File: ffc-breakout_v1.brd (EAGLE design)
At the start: 29.2 x 22.9 mm, 5 parts, among them X2 AMP_SFW16R-2STE1LF

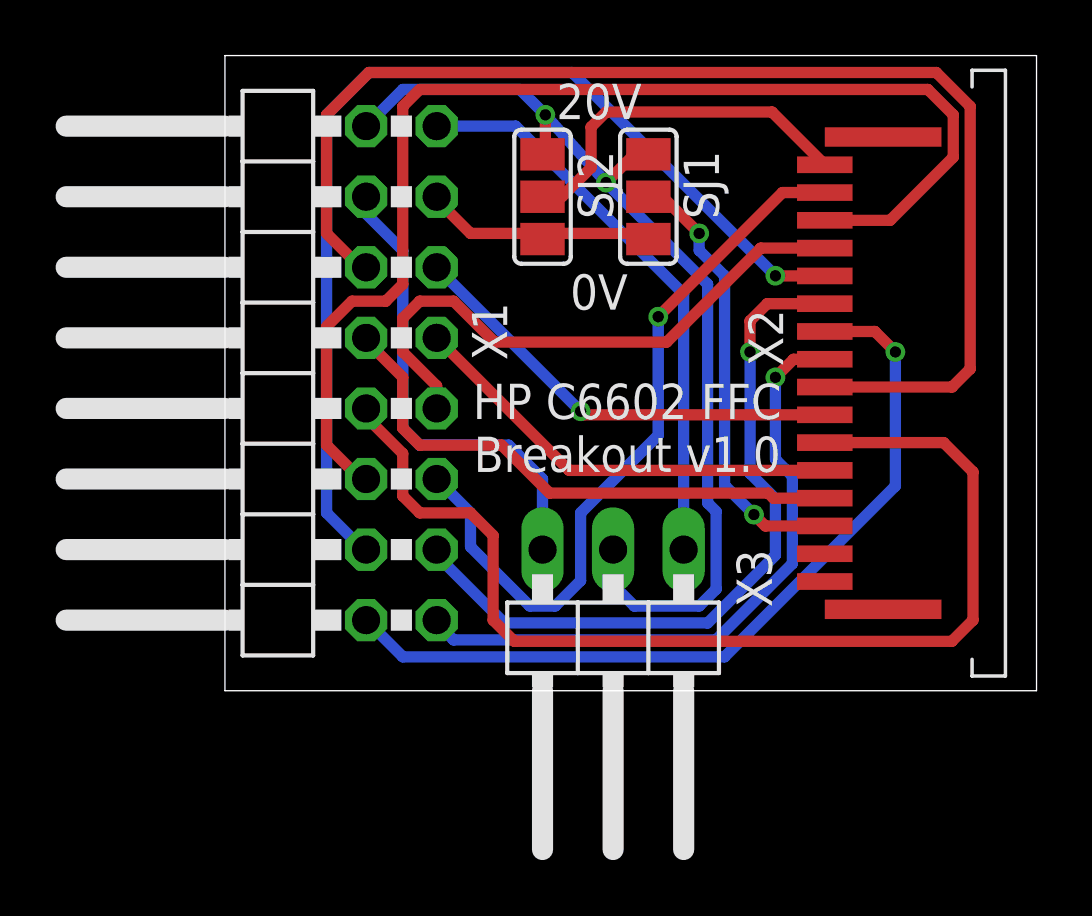
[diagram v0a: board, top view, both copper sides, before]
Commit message: BOM  + minor FFC update
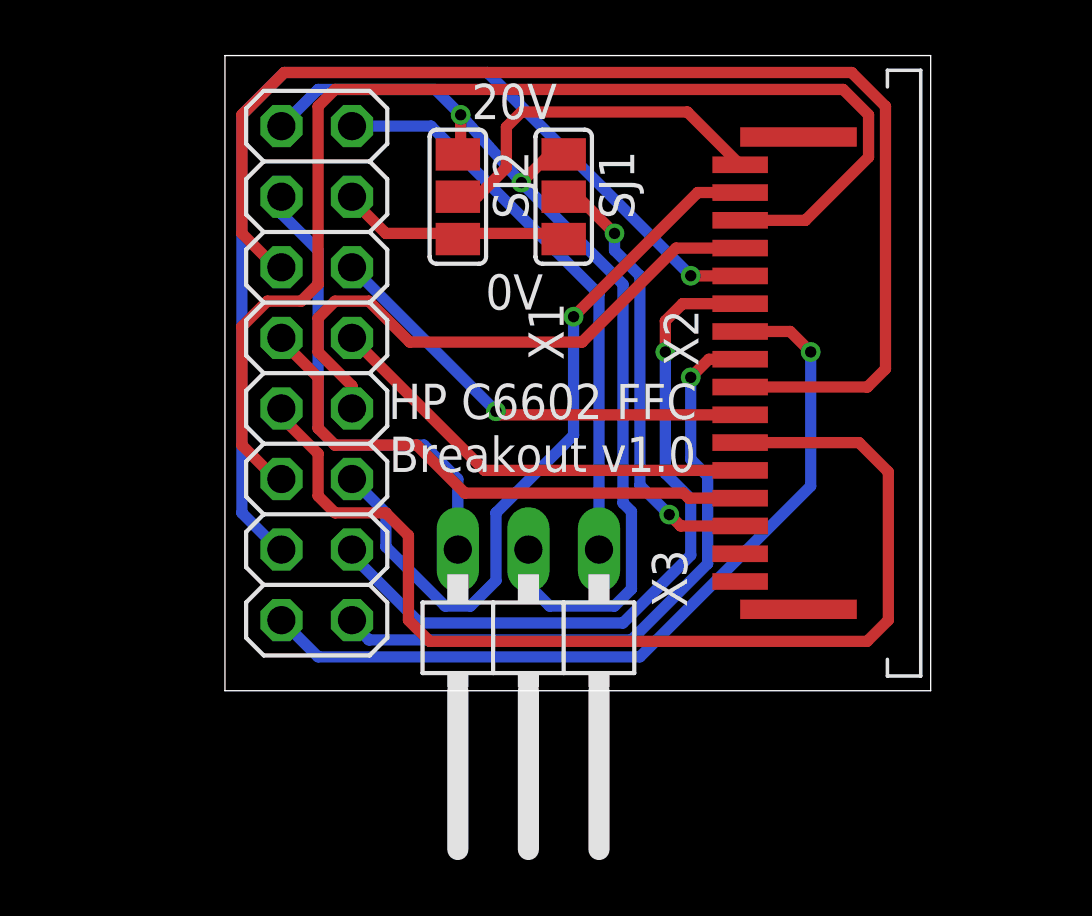
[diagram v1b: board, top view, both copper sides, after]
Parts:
- X1: device pinhead:2X08/90 -> pinhead:2X08
- moved SJ1 3.05 mm to (12.2, 17.8)
- moved SJ2 3.05 mm to (8.38, 17.8)
- moved X3 3.05 mm to (10.9, 1.27)
- moved X2 3.05 mm to (18.5, 11.4)
- moved X1 2.03 mm to (3.30, 11.4)
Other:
- board size 29.2 x 22.9 mm -> 25.4 x 22.9 mm
